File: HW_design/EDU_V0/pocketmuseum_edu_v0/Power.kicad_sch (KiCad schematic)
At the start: 15 parts, among them J101 USB_C_Receptacle_USB2.0_16P, U102 AMS1117-3.3

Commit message: Updated Readme
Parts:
- removed D103: LED, LED_SMD:LED_0402_1005Metric, symbol Device:LED
- removed R104: 2k, Resistor_SMD:R_0402_1005Metric, symbol Device:R
- added C1: 1u, Capacitor_SMD:C_0402_1005Metric, symbol Device:C
- added J102: JST PH S2B, Connector_JST:JST_PH_S2B-PH-SM4-TB_1x02-1MP_P2.00mm_Horizontal, symbol Connector:Conn_01x02_Socket
- added Q1: AO3401A, Package_TO_SOT_SMD:SOT-23, symbol Transistor_FET:AO3401A
- added R1: 10k, Resistor_SMD:R_0402_1005Metric, symbol Device:R
- added SW1: SW_SPDT, Button_Switch_SMD:SW_SPDT_PCM12, symbol Switch:SW_SPDT
- added U1: TLV740P18, Package_TO_SOT_SMD:SOT-23-5, symbol Regulator_Linear:TLV70018_SOT23-5
- added U2: TLV809EA29DBZ, Package_TO_SOT_SMD:SOT-23, symbol Power_Supervisor:TLV810EA29DBZ
- renumbered D2 to D102, D4 to D103
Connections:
- net GND: now also D101.2 (A2), D102.2 (A2), C1.2, J102.1 (Pin_1), U2.1 (GND); no longer D101.1 (A1), D102.1 (A1)
- net USB_D-: now also D102.1 (A1); no longer D102.2 (A2)
- net VBUS: no longer D101.2 (A2), J101.A4 (VBUS), J101.A9 (VBUS), J101.B4 (VBUS), J101.B9 (VBUS)
- net USB_CC2: now reaches J101.B5 (CC2), R101.1
- net USB_CC1: now reaches J101.A5 (CC1), R102.1
- new net UVLO_RST: Q1.1 (G), R1.1, U2.2 (RESET)
- new net VBAT: Q1.3 (D)
- new net VBAT_ALW_ON: C1.1, J102.2 (Pin_2), Q1.2 (S), R1.2, U2.3 (V_{DD})
- new net VUSB: D101.1 (A1), J101.A4 (VBUS), J101.A9 (VBUS), J101.B4 (VBUS), J101.B9 (VBUS)
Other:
- note added: "Battery Connector"
- note added: "Battery Under-Voltage Lockout"
- note added: "Under-Voltage-Lock-Out active: VBAT_ALW_ON < 2.93V TLV809E: push-ull active-low output"
- note removed: "Power LED If = 1mA"
- company: (none) -> Bucharest Applied STEAM Museum
- title: BASM POCKETMUSEUM EDU V0 -> POCKETMUSEUM EDU V0
- moved on the sheet: C101, C102, C105, C106, D102, D103, J101, L101, R101, R102, R106, U102

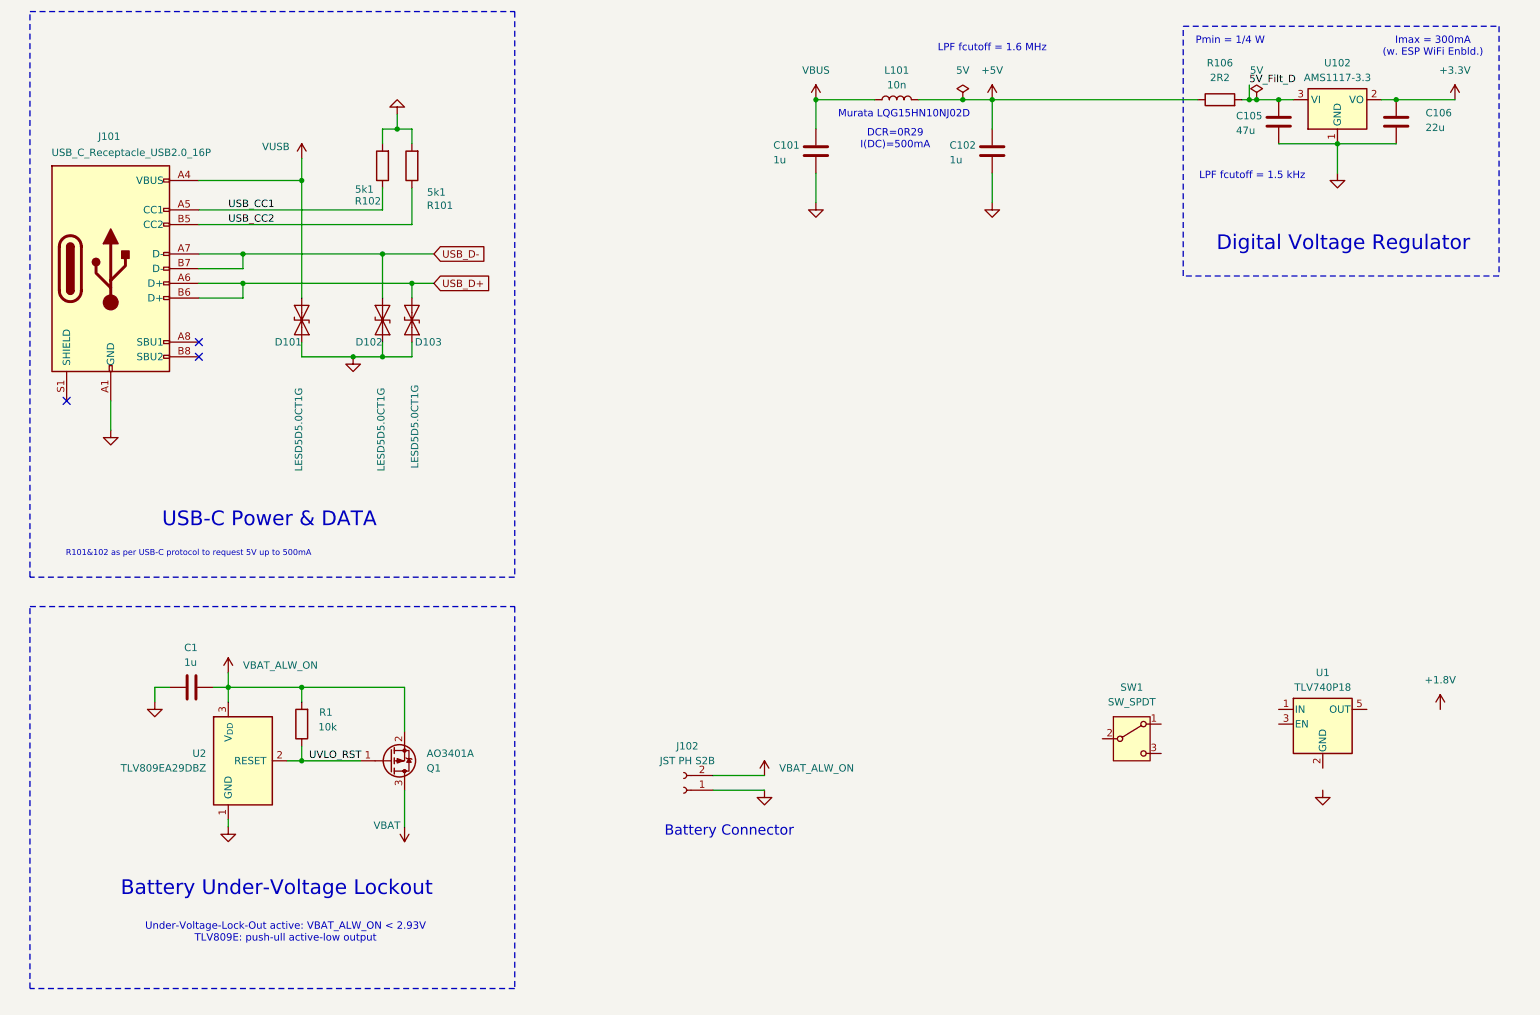
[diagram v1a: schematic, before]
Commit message: Added Mic & Light Sensor to EDU_V0
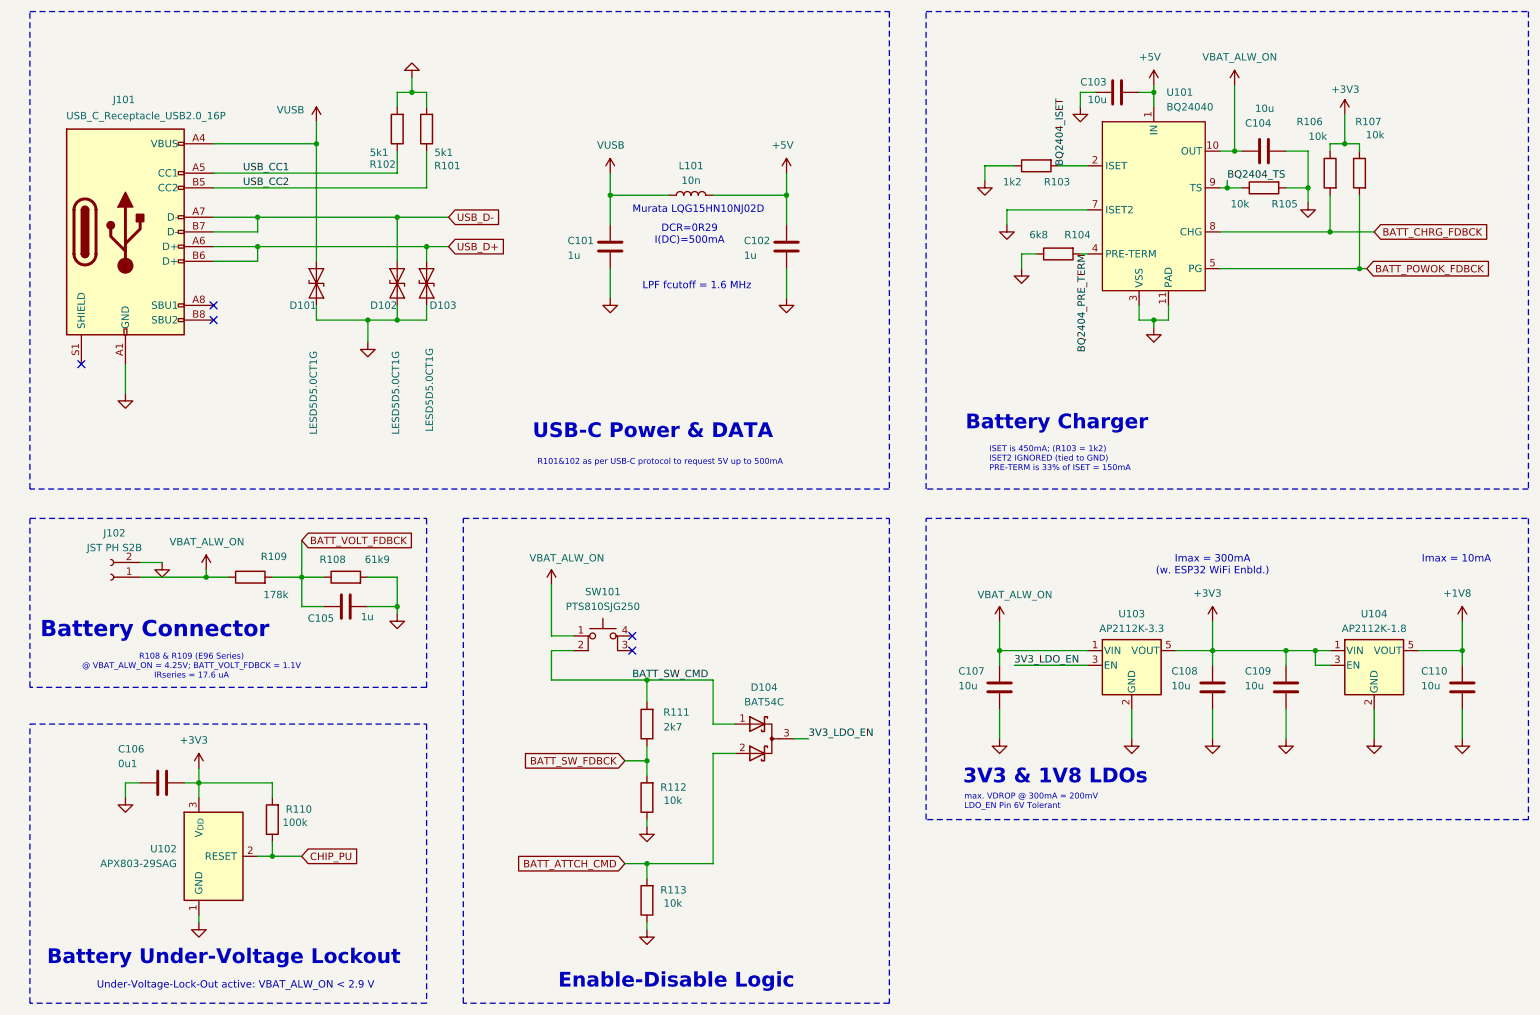
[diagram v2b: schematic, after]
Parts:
- removed C106: 22u, Capacitor_SMD:C_0603_1608Metric, symbol Device:C
- removed Q1: AO3401A, Package_TO_SOT_SMD:SOT-23, symbol Transistor_FET:AO3401A
- removed SW1: SW_SPDT, Button_Switch_SMD:SW_SPDT_PCM12, symbol Switch:SW_SPDT
- removed U1: TLV740P18, Package_TO_SOT_SMD:SOT-23-5, symbol Regulator_Linear:TLV70018_SOT23-5
- removed U102: AMS1117-3.3, Package_TO_SOT_SMD:SOT-223-3_TabPin2, symbol Regulator_Linear:AMS1117-3.3
- added C103, C104, C107, C108, C109, C110: 10u, Capacitor_SMD:C_0603_1608Metric, symbol Device:C
- added D104: BAT54C, Package_TO_SOT_SMD:SOT-23, symbol Device:D_Schottky_Dual_CommonCathode_AAK_Parallel
- added R103: 1k2, Resistor_SMD:R_0402_1005Metric, symbol Device:R
- added R104: 6k8, Resistor_SMD:R_0402_1005Metric, symbol Device:R
- added R105, R107, R112, R113: 10k, Resistor_SMD:R_0402_1005Metric, symbol Device:R
- added R108: 61k9, Resistor_SMD:R_0402_1005Metric, symbol Device:R
- added R109: 178k, Resistor_SMD:R_0402_1005Metric, symbol Device:R
- added R111: 2k7, Resistor_SMD:R_0402_1005Metric, symbol Device:R
- added SW101: PTS810SJG250, Button_Switch_SMD:SW_SPST_PTS810, symbol Switch:SW_MEC_5E
- added U101: BQ24040, DFNCustom:QFN-10_EP_2.1x2.1_Pitch0.4mm, symbol BQ240x:BQ24040
- added U103: AP2112K-3.3, Package_TO_SOT_SMD:SOT-23-5, symbol Regulator_Linear:AP2112K-3.3
- added U104: AP2112K-1.8, Package_TO_SOT_SMD:SOT-23-5, symbol Regulator_Linear:AP2112K-1.8
- C105: value 47u -> 1u; footprint Capacitor_SMD:C_0603_1608Metric -> Capacitor_SMD:C_0402_1005Metric; JLCPCB Link https://jlcpcb.com/partdetail/152108-GRM188R60J476ME15D/C14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 -> https://jlcpcb.com/partdetail/15107-CL05A105KP5NNNC/C14445; Manufacturer Murata Electronics -> Samsung Electro-Mechanics; Manufacturer P/N GRM188R60J476ME15D -> CL05A105KP5NNNC
- C106: renamed from C1; value 1u -> 0u1
- R106: value 2R2 -> 10k; footprint Resistor_SMD:R_1206_3216Metric -> Resistor_SMD:R_0402_1005Metric; JLCPCB Link https://jlcpcb.com/partdetail/18635-1206W4F220KT5E/C17947 -> https://jlcpcb.com/partdetail/26648-0402WGF5101TCE/C25905; Manufacturer P/N 1206W4F220KT5E -> 0402WGF5101TCE
- R110: renamed from R1; value 10k -> 100k
- U102: renamed from U2; value TLV809EA29DBZ -> APX803-29SAG
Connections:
- net VBUS is gone; now on net VUSB: C101.1, L101.1
- net +5V: now also C103.1, U101.1 (IN); no longer R106.1
- net GND: now also J102.2 (Pin_2), C103.2, C104.2, C107.2, C108.2, C109.2, C110.2, R103.1, R104.1, R105.2, R108.2, R112.1, R113.1, U101.11 (PAD), U101.3 (VSS), U101.7 (ISET2), U103.2 (GND), U104.2 (GND); no longer J102.1 (Pin_1)
- net VBAT_ALW_ON: now also J102.1 (Pin_1), C104.1, C107.1, R109.1, SW101.1, U101.10 (OUT), U103.1 (VIN); no longer C106.1, J102.2 (Pin_2), R110.2, U102.3 (V_{DD})
- net 5V_Filt_D renamed BATT_CHRG_FDBCK
- net BATT_CHRG_FDBCK: now also U101.8 (CHG); no longer C105.1
- net UVLO_RST renamed CHIP_PU
- new net +1V8: C110.1, U104.5 (VOUT)
- new net +3V3: C106.1, C108.1, C109.1, R106.1, R107.1, R110.2, U102.3 (V_{DD}), U103.5 (VOUT), U104.1 (VIN), U104.3 (EN)
- new net 3V3_LDO_EN: D104.3 (K), U103.3 (EN)
- new net BATT_ATTCH_CMD: D104.2 (A), R113.2
- new net BATT_POWOK_FDBCK: R107.2, U101.5 (PG)
- new net BATT_SW_CMD: D104.1 (A), R111.2, SW101.2
- new net BATT_SW_FDBCK: R111.1, R112.2
- new net BATT_VOLT_FDBCK: C105.1, R108.1, R109.2
- new net BQ2404_ISET: R103.2, U101.2 (ISET)
- new net BQ2404_PRE_TERM: R104.2, U101.4 (PRE-TERM)
- new net BQ2404_TS: R105.1, U101.9 (TS)
- no-connect marks 3 -> 5
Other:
- note added: "3V3 & 1V8 LDOs"
- note added: "Battery Charger"
- note added: "Enable-Disable Logic"
- note added: "ISET is 450mA; (R103 = 1k2) ISET2 IGNORED (tied to GND) PRE-TERM is 33% of ISET = 150mA"
- note added: "Imax = 10mA"
- note added: "Imax = 300mA (w. ESP32 WiFi Enbld.)"
- note added: "R108 & R109 (E96 Series) @ VBAT_ALW_ON = 4.25V; BATT_VOLT_FDBCK = 1.1V IRseries = 17.6 uA"
- note added: "Under-Voltage-Lock-Out active: VBAT_ALW_ON < 2.9 V"
- note added: "max. VDROP @ 300mA = 200mV LDO_EN Pin 6V Tolerant"
- note removed: "Digital Voltage Regulator"
- note removed: "Imax = 300mA (w. ESP WiFi Enbld.)"
- note removed: "LPF fcutoff = 1.5 kHz"
- note removed: "Pmin = 1/4 W"
- note removed: "Under-Voltage-Lock-Out active: VBAT_ALW_ON < 2.93V TLV809E: push-ull active-low output"
- moved on the sheet: C102, C106, D101, D102, D103, J101, L101, R101, R102, R110, U102

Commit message: Diagram review complete
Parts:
- added R114: 0R, Resistor_SMD:R_0603_1608Metric, symbol Device:R
- R111: value 2k7 -> 3k3
- U101: footprint DFNCustom:QFN-10_EP_2.1x2.1_Pitch0.4mm -> DFNCustom:QFN_10_BQ24040
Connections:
- net GND: now also R114.2
- net at J101.S1 (SHIELD): now also R114.1
- no-connect marks 5 -> 4
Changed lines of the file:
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@@
 	)
 	(no_connect
-		(at 27.94 81.28)
-	)
-	(no_connect
 		(at 50.8 73.66)
 	)
@@
 	(wire
 		(pts
+			(xy 27.94 92.71) (xy 27.94 88.9)
+		)
+		(stroke
+			(width 0)
+			(type default)
+		)
+	)
+	(wire
+		(pts
 			(xy 82.55 48.26) (xy 82.55 44.45)
 		)
@@
 	(text "ISET is 450mA; (R103 = 1k2)\nISET2 IGNORED (tied to GND)\nPRE-TERM is 33% of ISET = 150mA\n\n"
 		(exclude_from_sim no)
-		(at 184.912 98.552 0)
+		(at 182.118 99.06 0)
 		(effects
 			(font
@@
 	(text "R108 & R109 (E96 Series)\n@ VBAT_ALW_ON = 4.25V; BATT_VOLT_FDBCK = 1.1V\nIRseries = 17.6 uA"
 		(exclude_from_sim no)
-		(at 46.99 133.604 0)
+		(at 28.448 133.096 0)
 		(effects
 			(font
 				(size 1.016 1.016)
 			)
+			(justify left)
 		)
 	)
@@
 			)
 		)
-		(property "Footprint" "DFNCustom:QFN-10_EP_2.1x2.1_Pitch0.4mm"
+		(property "Footprint" "DFNCustom:QFN_10_BQ24040"
 			(at 213.36 55.88 0)
 			(effects
@@
 			)
 		)
-		(property "Value" "2k7"
+		(property "Value" "3k3"
 			(at 131.826 144.018 0)
 			(effects
@@
 	(symbol
 		(lib_id "power:GND")
+		(at 27.94 92.71 0)
+		(unit 1)
+		(exclude_from_sim no)
+		(in_bom yes)
+		(on_board yes)
+		(dnp no)
+		(fields_autoplaced yes)
+		(property "Reference" "#PWR0115"
+			(at 27.94 99.06 0)
+			(effects
+				(font
+					(size 1.27 1.27)
+				)
+				(hide yes)
+			)
+		)
+		(property "Value" "GND"
+			(at 27.94 97.79 0)
+			(effects
+				(font
+					(size 1.27 1.27)
+				)
+				(hide yes)
+			)
+		)
+		(property "Footprint" ""
+			(at 27.94 92.71 0)
+			(effects
+				(font
+					(size 1.27 1.27)
+				)
+				(hide yes)
+			)
+		)
+		(property "Datasheet" ""
+			(at 27.94 92.71 0)
+			(effects
+				(font
+					(size 1.27 1.27)
+				)
+				(hide yes)
+			)
+		)
+		(property "Description" "Power symbol creates a global label with name \"GND\" , ground"
+			(at 27.94 92.71 0)
+			(effects
+				(font
+					(size 1.27 1.27)
+				)
+				(hide yes)
+			)
+		)
+		(pin "1"
+		)
+		(instances
+			(project "pocketmuseum_edu_v0"
+				(path "/4bede6f6-420d-49b9-8d53-bd69095749c2/17afeba3-86f9-4a78-9898-2f2df319c871"
+					(reference "#PWR0115")
+					(unit 1)
+				)
+			)
+		)
+	)
+	(symbol
+		(lib_id "power:GND")
 		(at 236.22 146.05 0)
 		(unit 1)
@@
 					(unit 1)
 				)
+			)
+		)
+	)
+	(symbol
+		(lib_id "Device:R")
+		(at 27.94 85.09 0)
+		(unit 1)
+		(exclude_from_sim no)
+		(in_bom yes)
+		(on_board yes)
+		(dnp no)
+		(property "Reference" "R114"
+			(at 31.496 83.566 90)
+			(effects
+				(font
+					(size 1.27 1.27)
+				)
+			)
+		)
+		(property "Value" "0R"
+			(at 31.496 88.138 90)
+			(effects
+				(font
+					(size 1.27 1.27)
+				)
+			)
+		)
+		(property "Footprint" "Resistor_SMD:R_0603_1608Metric"
+			(at 26.162 85.09 90)
+			(effects
+				(font
+					(size 1.27 1.27)
+				)
+				(hide yes)
+			)
+		)
+		(property "Datasheet" "~"
+			(at 27.94 85.09 0)
+			(effects
+				(font
+					(size 1.27 1.27)
+				)
+				(hide yes)
+			)
+		)
+		(property "Description" "Resistor"
+			(at 27.94 85.09 0)
+			(effects
+				(font
+					(size 1.27 1.27)
+				)
+				(hide yes)
+			)
+		)
+		(property "JLCPCB Link" "https://jlcpcb.com/partdetail/16080-0603WAJ0000T5E/C15402"
+			(at 27.94 85.09 0)
+			(effects
+				(font
+					(size 1.27 1.27)
+				)
+				(hide yes)
+			)
+		)
+		(property "Manufacturer" "UNI-ROYAL(Uniroyal Elec) "
+			(at 27.94 85.09 0)
+			(effects
+				(font
+					(size 1.27 1.27)
+				)
+				(hide yes)
+			)
+		)
+		(property "Manufacturer P/N" "0603WAJ0000T5E"
+			(at 27.94 85.09 0)
+			(effects
+				(font
+					(size 1.27 1.27)
+				)
+				(hide yes)
+			)
+		)
+		(pin "2"
+		)
+		(pin "1"
+		)
+		(instances
+			(project "pocketmuseum_edu_v0"
+				(path "/4bede6f6-420d-49b9-8d53-bd69095749c2/17afeba3-86f9-4a78-9898-2f2df319c871"
+					(reference "R114")
+					(unit 1)
+				)

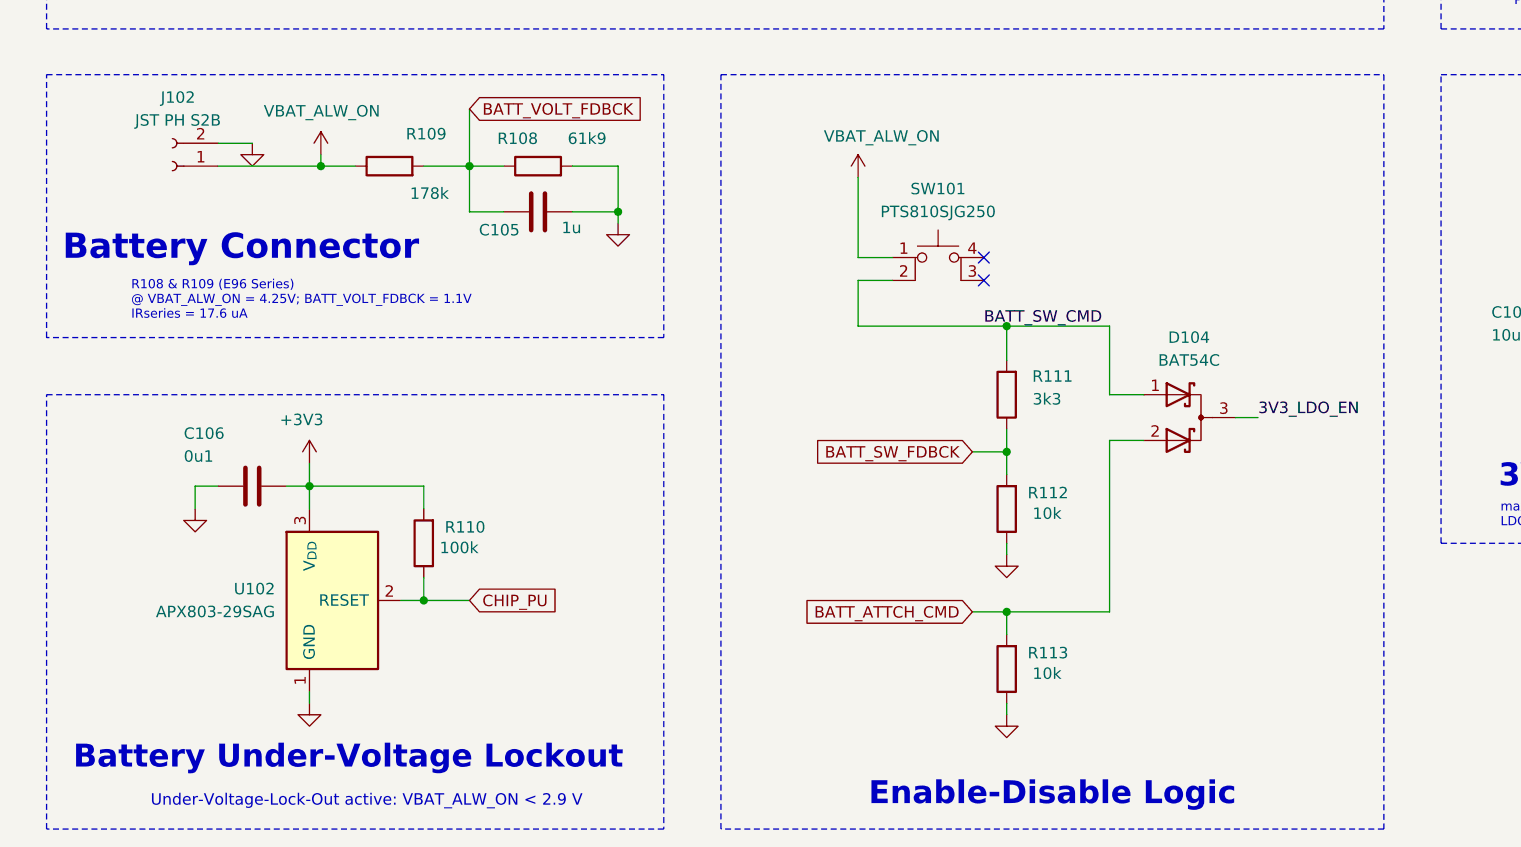
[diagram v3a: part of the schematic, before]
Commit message: EDUV0 added TP n routing in progress
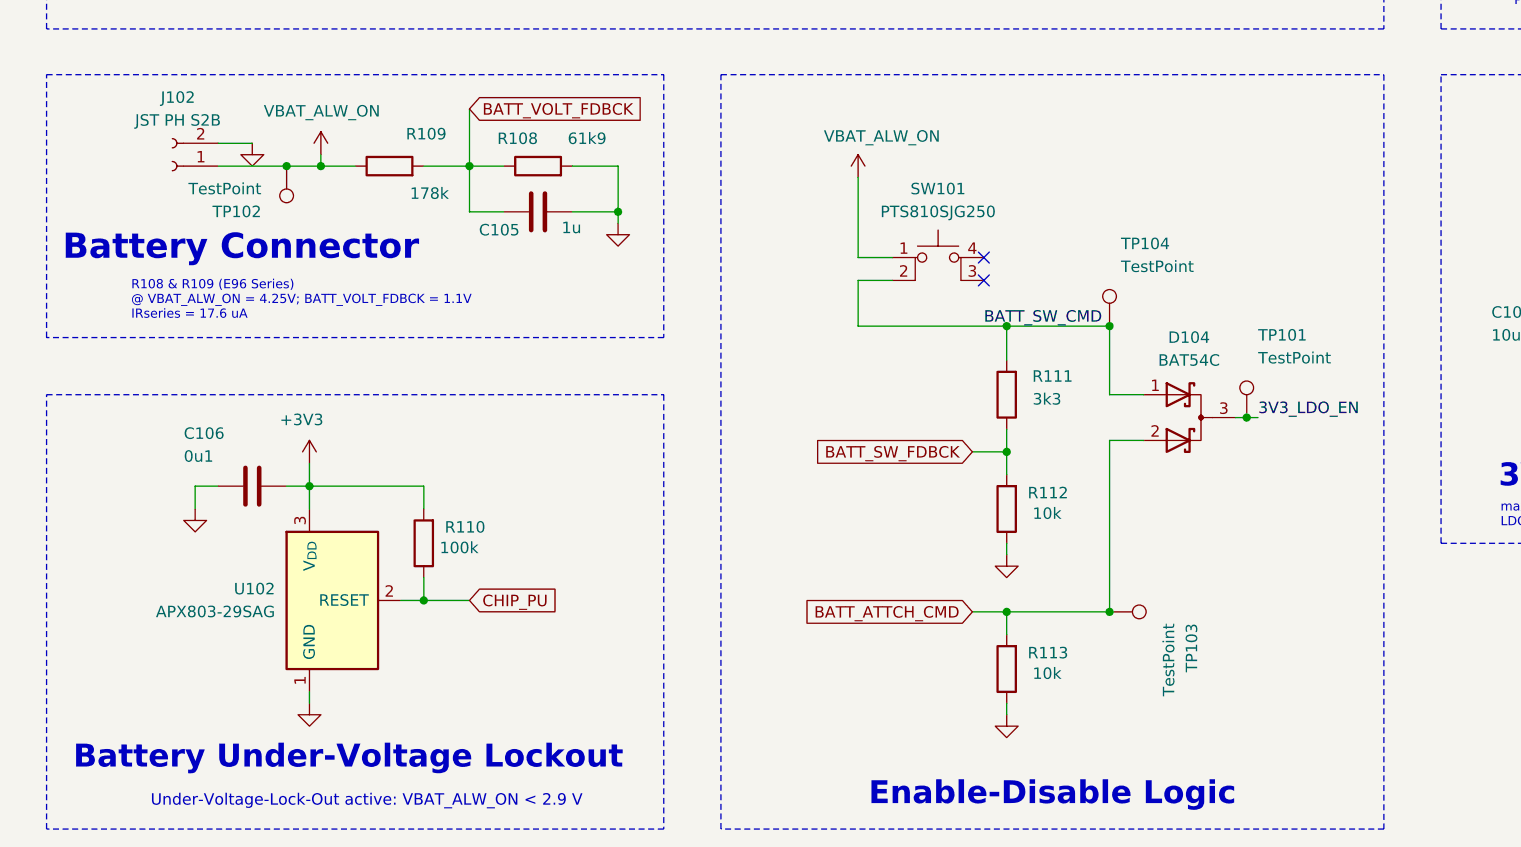
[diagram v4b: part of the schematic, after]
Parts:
- added TP101, TP102, TP103, TP104: TestPoint, TestPoint:TestPoint_Pad_D2.0mm, symbol Connector:TestPoint
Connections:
- net 3V3_LDO_EN: now also TP101.1
- net BATT_ATTCH_CMD: now also TP103.1
- net BATT_SW_CMD: now also TP104.1
- net VBAT_ALW_ON: now also TP102.1

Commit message: EDUV0 Production Files
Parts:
- added TP105: TestPoint, TestPoint:TestPoint_Pad_D2.0mm, symbol Connector:TestPoint
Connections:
- net +1V8: now also TP105.1
